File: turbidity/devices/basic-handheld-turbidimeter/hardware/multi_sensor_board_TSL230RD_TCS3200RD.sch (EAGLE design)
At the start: 5 parts

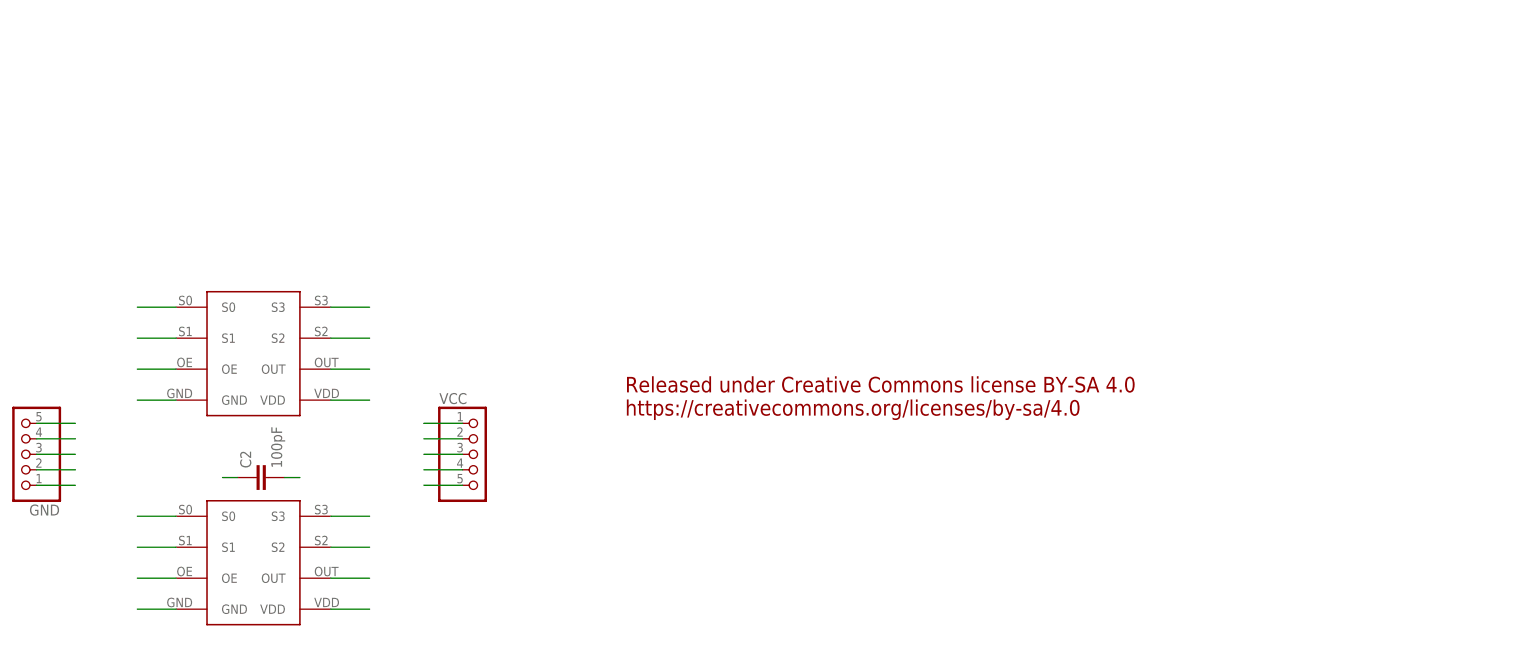
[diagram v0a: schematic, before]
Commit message: Improved Multi Sensor Board Schematic
All nets were visibly labeled to allow for easy readability.  PDF was
also updated with the new schematic.
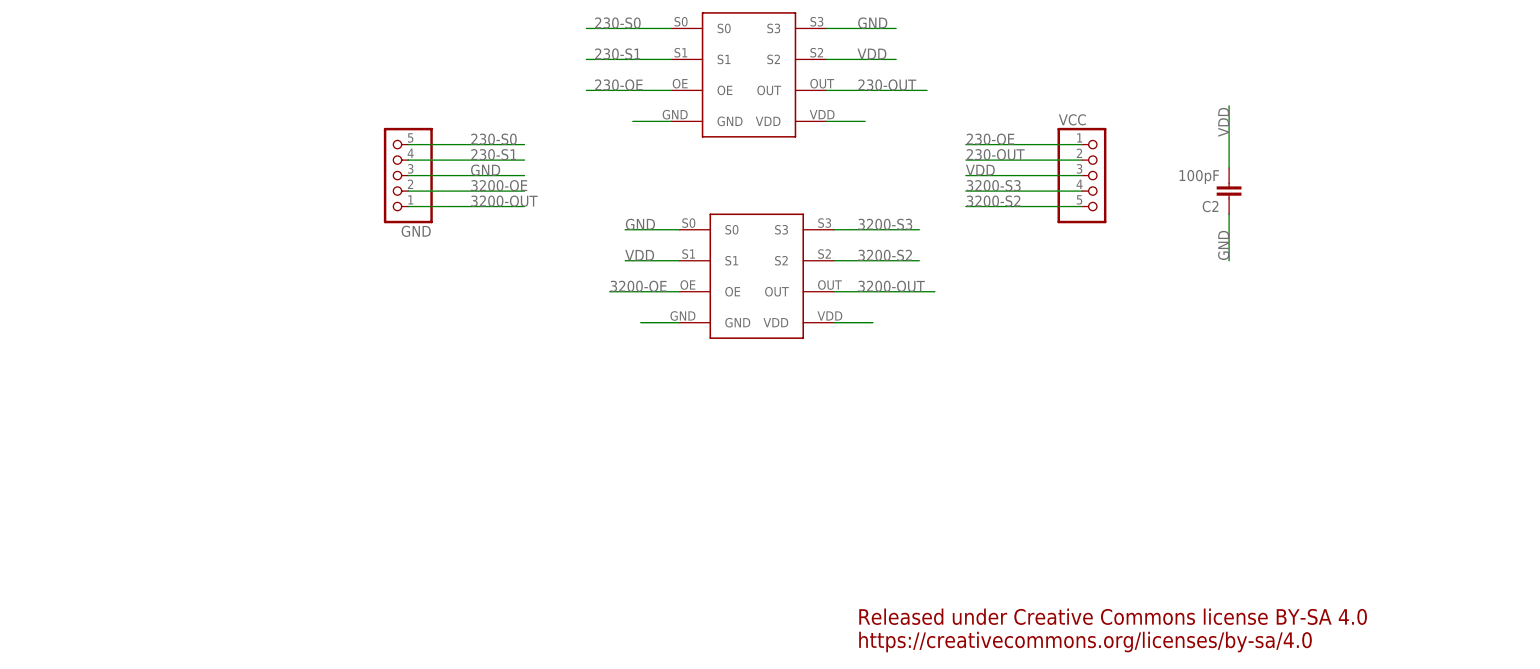
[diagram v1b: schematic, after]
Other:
- moved on the sheet: C2, GND, VCC
